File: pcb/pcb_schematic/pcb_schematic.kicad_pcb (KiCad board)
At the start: 2 copper layers, 35 parts, among them J1 Conn_ST_STDC14, J2 USB_B_Micro, J3 Conn_02x02_Odd_Even, Q1 MMBT3904, Q2 MMBT3904, Q3 MMBT3904, U1 STM32G031K8Tx, U2 MIC5301-3.3YD5, U4 SSD1306 128 x 64 OLED (0x3C), Y1 Crystal

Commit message: the schmatic keeps chaning i wanna cry
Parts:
- removed C10, C7: 1uF CER, Capacitor_SMD:C_0805_2012Metric
- removed C5: 4.7nF 1KV, Capacitor_SMD:C_0805_2012Metric
- removed C9: 0.01uF, Capacitor_SMD:C_0805_2012Metric
- removed J2: USB_B_Micro, Connector_USB:USB_Micro-B_Amphenol_10118194_Horizontal
- removed R1: 1M, Resistor_SMD:R_0805_2012Metric
- removed R11: 10K, Resistor_SMD:R_0805_2012Metric
- removed R3: 1.1k, Resistor_SMD:R_0805_2012Metric
- removed R4: 330, Resistor_SMD:R_0805_2012Metric
- added C14: 10uF, Capacitor_SMD:C_0805_2012Metric, F.Cu at (184.7, 119.6)
- added C6: 4.7nF 1KV, Capacitor_SMD:C_0805_2012Metric, F.Cu at (180.2, 116.6)
- added C8: 10uF, Capacitor_SMD:C_0805_2012Metric, F.Cu at (180.2, 119.6)
- added D1: CLMVC-FKA-CLBDGL7LBB79353, RGB_LED:LED_CLMVC-FKA-CLBDGL7LBB79353, F.Cu at (148.3, 41.6)
- added J4: USB_B_Micro, Connector_USB:USB_Micro-B_Amphenol_10118194_Horizontal, F.Cu at (178.2, 75.0)
- added R12: 10K, Resistor_SMD:R_0805_2012Metric, F.Cu at (178.0, 105.8)
- added U5: TCS34725 (0x29), Sensor:TCS34725, F.Cu at (149.8, 73.4)
- R2: value 1k -> 1M
- R5: value 1k -> 470
- R6: value 1.1k -> 220
- R7: value 330 -> 51
- U2: value MIC5301-3.3YD5 -> NCP1117-3.3_SOT223; footprint Package_TO_SOT_SMD:TSOT-23-5 -> Package_TO_SOT_SMD:SOT-223-3_TabPin2
- moved H1 165.5 mm to (274.7, 20.4)
- moved H2 165.5 mm to (274.7, 28.3)
- moved H3 165.5 mm to (274.7, 36.2)
- moved H4 165.5 mm to (274.7, 44.2)
- moved R10 74.4 mm to (178.0, 102.8)
- moved R8 74.4 mm to (178.0, 96.9)
- moved R9 74.4 mm to (178.0, 99.9)
- moved U2 67.9 mm to (185.1, 106.4)
- moved Y1 53.7 mm to (112.0, 75.7), turned to 90 degrees
- moved R5 52.1 mm to (149.0, 48.3)
- moved R6 52.1 mm to (149.0, 51.3)
- moved R7 52.1 mm to (149.0, 54.2)
- moved C11 51.2 mm to (184.7, 113.6)
- moved C12 51.2 mm to (184.7, 116.6)
- moved Q1 45.5 mm to (143.6, 46.7)
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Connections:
- Q2 pad 1: unconnected-(Q2-B-Pad1) -> Net-(Q2-B)
- Q3 pad 1: unconnected-(Q3-B-Pad1) -> Net-(Q3-B)
- R10 pad 2: unconnected-(R10-Pad2) -> Net-(Q3-B)
- R2 pad 1: unconnected-(R2-Pad1) -> Net-(J4-Shield)
- R2 pad 2: unconnected-(R2-Pad2) -> GND
- R9 pad 2: unconnected-(R9-Pad2) -> Net-(Q2-B)
- U1 pad 13: PWM1 -> unconnected-(U1-PA6-Pad13)
- U1 pad 14: PWM2 -> unconnected-(U1-PA7-Pad14)
- U1 pad 18: PWM3 -> PWM1
- U1 pad 22: unconnected-(U1-PA9/PA11-Pad22) -> PWM2
- U1 pad 23: unconnected-(U1-PA10/PA12-Pad23) -> PWM3
- U2 pad 1: VBUS -> GND
- U2 pad 2: GND -> +3.3V
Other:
- board outline added: 20.3 x 20.3 mm

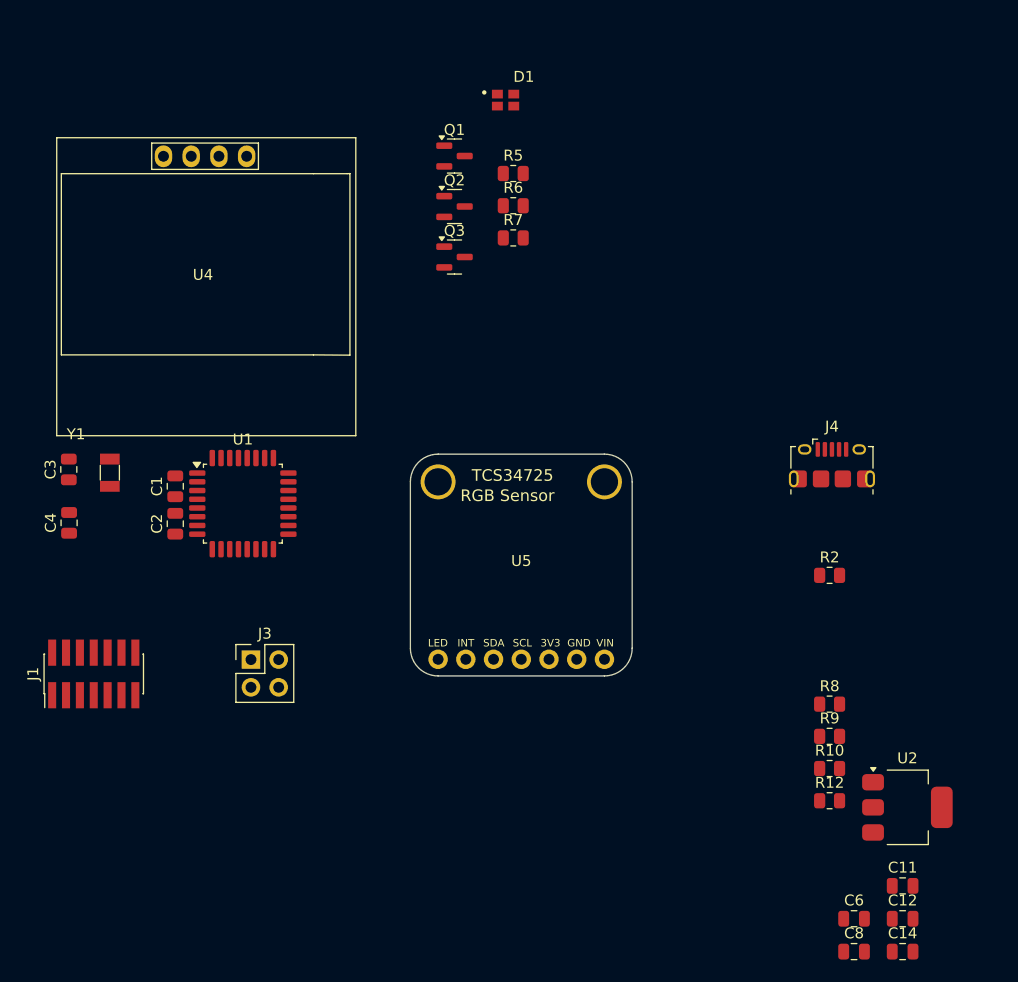
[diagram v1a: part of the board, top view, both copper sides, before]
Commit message: Components are laid out
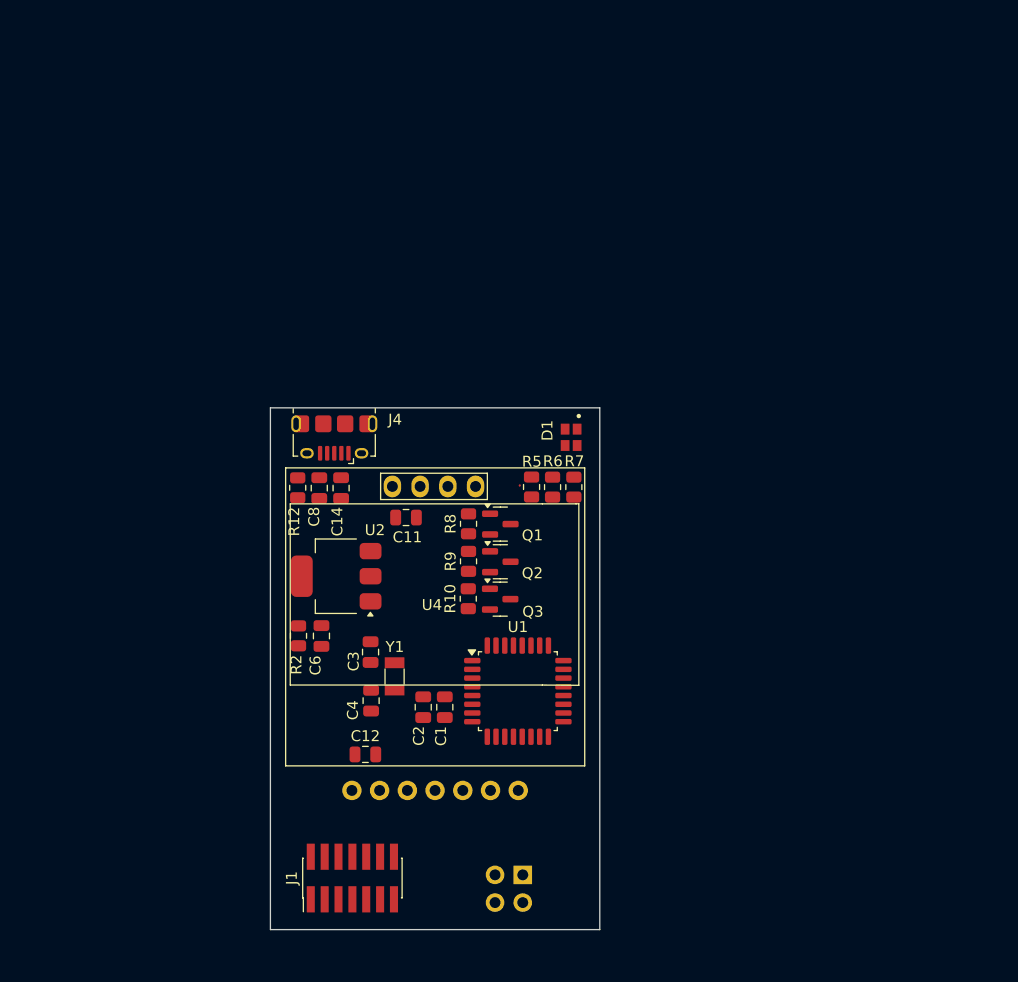
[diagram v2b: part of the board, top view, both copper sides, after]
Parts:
- J3, U5: moved to B.Cu
- moved C14 66.7 mm to (133.2, 77.1), turned to -90 degrees
- moved C8 64.8 mm to (131.2, 77.1), turned to 90 degrees
- moved C11 56.6 mm to (139.2, 79.8), turned to 180 degrees
- moved R12 56.5 mm to (129.2, 77.1), turned to 90 degrees
- moved U2 56.5 mm to (132.8, 85.2), turned to 180 degrees
- moved C6 55.2 mm to (131.4, 90.7), turned to 90 degrees
- moved C12 51.5 mm to (135.4, 101.5)
- moved R2 49.0 mm to (129.3, 90.7), turned to 90 degrees
- moved J4 45.7 mm to (132.6, 72.5), turned to 180 degrees
- moved R8 37.0 mm to (144.9, 80.4), turned to 90 degrees
- moved U4 36.8 mm to (141.5, 87.6)
- moved R9 36.8 mm to (144.9, 83.8), turned to 90 degrees
- moved R10 36.6 mm to (144.9, 87.3), turned to 90 degrees
- moved Q1 34.0 mm to (147.8, 80.4)
- moved Q2 32.8 mm to (147.8, 83.9)
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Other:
- board size 20.3 x 20.3 mm -> 30.2 x 47.8 mm
- copper layers 2 -> 4

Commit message: Update pcb_schematic.kicad_pcb
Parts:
- moved R8 39.3 mm to (183.7, 86.6)
- moved Q1 36.8 mm to (184.6, 83.0), turned to 90 degrees
- moved R9 35.5 mm to (180.2, 86.6)
- moved R12 34.3 mm to (163.5, 79.3)
- moved C8 34.3 mm to (165.5, 79.3)
- moved R5 33.9 mm to (184.5, 79.2)
- moved R2 33.8 mm to (161.1, 79.2), turned to -90 degrees
- moved Q2 33.3 mm to (181.1, 83.0), turned to 90 degrees
- moved U2 32.0 mm to (164.7, 87.0)
- moved R10 31.8 mm to (176.6, 86.6)
- moved J1 31.4 mm to (165.6, 114.1)
- moved J3 31.4 mm to (181.2, 113.8)
- moved Y1 30.2 mm to (168.3, 94.6)
- moved Q3 30.1 mm to (177.6, 83.0), turned to 90 degrees
- moved C4 30.1 mm to (166.1, 96.8)
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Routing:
- net Net-(J4-Shield): track 0.00 -> 17.2 mm
- net PWM1: track 0.00 -> 15.0 mm
- net PWM3: track 0.00 -> 13.9 mm
- net PWM2: track 0.00 -> 13.0 mm
- net GND: track 0.00 -> 12.9 mm, vias 0 -> 1
- net +3.3V: track 0.00 -> 11.1 mm
- net Net-(U1-PC14): track 0.00 -> 9.97 mm
- net Net-(U1-PC15): track 0.00 -> 9.82 mm
- net Net-(D1-Pad4): track 0.00 -> 8.75 mm
- net INT: track 0.00 -> 6.23 mm
- net LED: track 0.00 -> 5.84 mm
- net Net-(D1-Pad3): track 0.03 -> 4.79 mm
- net VBUS: track 0.00 -> 4.28 mm
- net Net-(D1-Pad2): track 0.00 -> 2.89 mm
- net Net-(Q1-C): track 0.00 -> 1.94 mm
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- added copper zone on In1.Cu, net GND

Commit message: Update pcb_schematic.kicad_pcb
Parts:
- moved C14 9.83 mm to (168.2, 86.3), turned to 90 degrees
- moved U2 2.78 mm to (162.6, 85.2)
- moved C1 0.83 mm to (172.5, 98.6)
- moved C2 0.83 mm to (170.5, 98.6)
- moved C3 0.83 mm to (166.0, 93.1)
- moved Y1 0.83 mm to (168.3, 95.4)
- moved C4 0.83 mm to (166.1, 97.6)
- moved U1 0.83 mm to (179.3, 98.0)
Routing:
- net SCL: track 0.00 -> 49.9 mm, vias 0 -> 2
- net SDA: track 0.00 -> 49.9 mm, vias 0 -> 1
- net GND: track 12.9 -> 35.0 mm, vias 1 -> 15
- net Net-(J1-~{RST}): track 0.00 -> 12.2 mm, vias 0 -> 1
- net +3.3V: track 11.1 -> 19.4 mm, vias 0 -> 4
- net Net-(J3-Pin_3): track 0.00 -> 7.48 mm, vias 0 -> 2
- net VBUS: track 4.28 -> 9.58 mm
- added copper zone on In2.Cu, net +3.3V

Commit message: Update pcb_schematic.kicad_pcb
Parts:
- moved J3 5.75 mm to (175.6, 112.8), turned to -90 degrees
- moved J1 2.40 mm to (168.0, 114.1)
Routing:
- net Net-(J1-JCLK/SWCLK): track 0.00 -> 34.9 mm, vias 0 -> 2
- net Net-(J1-JTMS/SWDIO): track 0.14 -> 31.6 mm, vias 0 -> 2
- net Net-(J3-Pin_1): track 0.00 -> 11.1 mm, vias 0 -> 1
- net Net-(J1-VCP_RX): track 0.00 -> 10.3 mm, vias 0 -> 1
- net +3.3V: track 19.4 -> 28.6 mm, vias 4 -> 6
- net Net-(J1-~{RST}): track 12.2 -> 18.2 mm, vias 1 -> 0
- net Net-(J1-VCP_TX): track 0.00 -> 5.54 mm, vias 0 -> 2
- net GND: track 35.0 -> 40.4 mm, vias 15 -> 18
- net Net-(J3-Pin_3): track 7.48 -> 11.1 mm, vias 2 -> 1
- net INT: track 6.23 -> 7.30 mm
- net LED: track 5.84 -> 5.01 mm
- net PWM3: track 14.2 -> 14.8 mm
- net Net-(J4-Shield): track 17.0 -> 17.6 mm

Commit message: before i change many thing
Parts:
- moved H3 144.0 mm to (154.5, 115.5)
- moved H1 131.9 mm to (154.5, 74.7)
- moved H4 111.6 mm to (188.8, 115.5)
- moved H2 97.5 mm to (188.9, 74.7)
- moved C6 2.64 mm to (156.7, 80.4)
- moved R2 0.83 mm to (160.2, 79.2)
- moved U2 0.65 mm to (162.8, 85.8)
- moved J4 0.35 mm to (162.4, 74.2)
- moved C14 0.24 mm to (168.4, 86.3)
- moved D1 0.18 mm to (184.2, 74.6)
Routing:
- net Net-(J4-Shield): track 17.6 -> 12.3 mm
- net GND: track 40.4 -> 39.4 mm
- net +3.3V: track 28.6 -> 28.1 mm
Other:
- board size 30.2 x 47.8 mm -> 41.4 x 47.8 mm
- board text added: "Jaedyn Carbonell CMPE2750 RGB Reader"

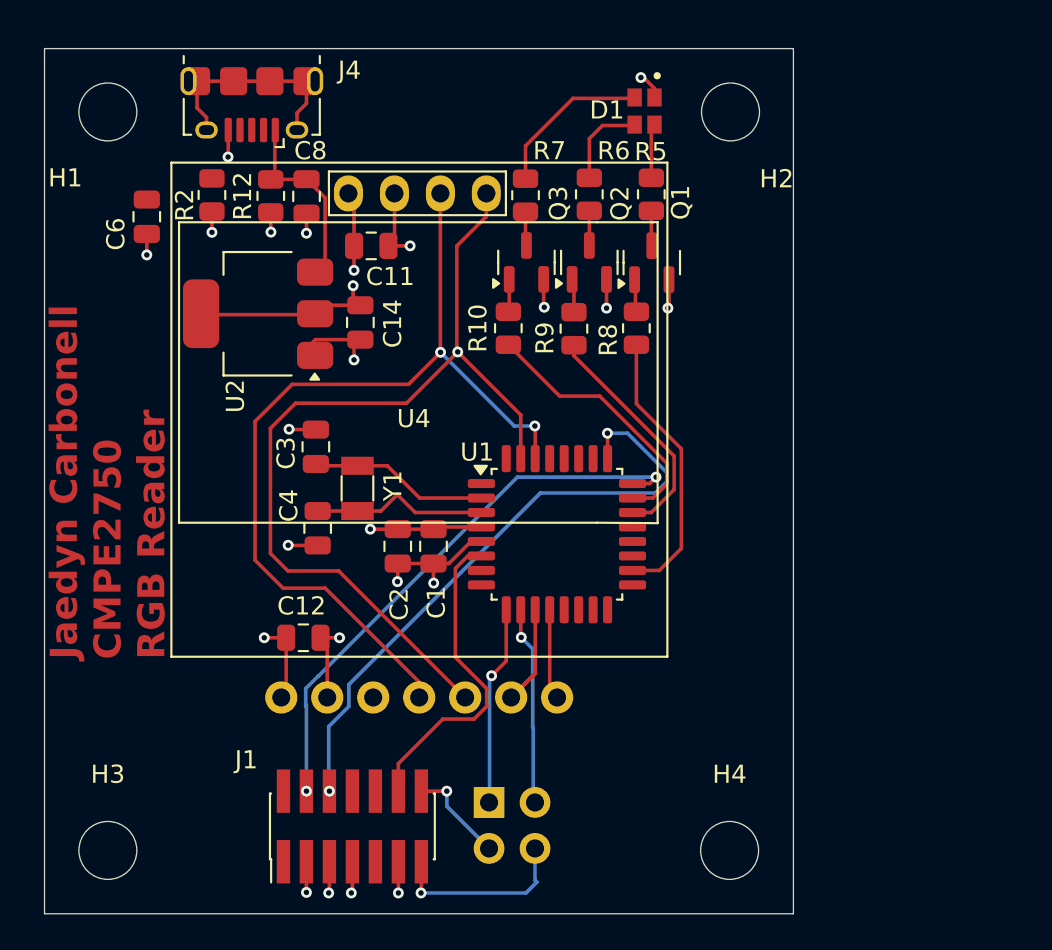
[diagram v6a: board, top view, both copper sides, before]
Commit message: moved rbg led
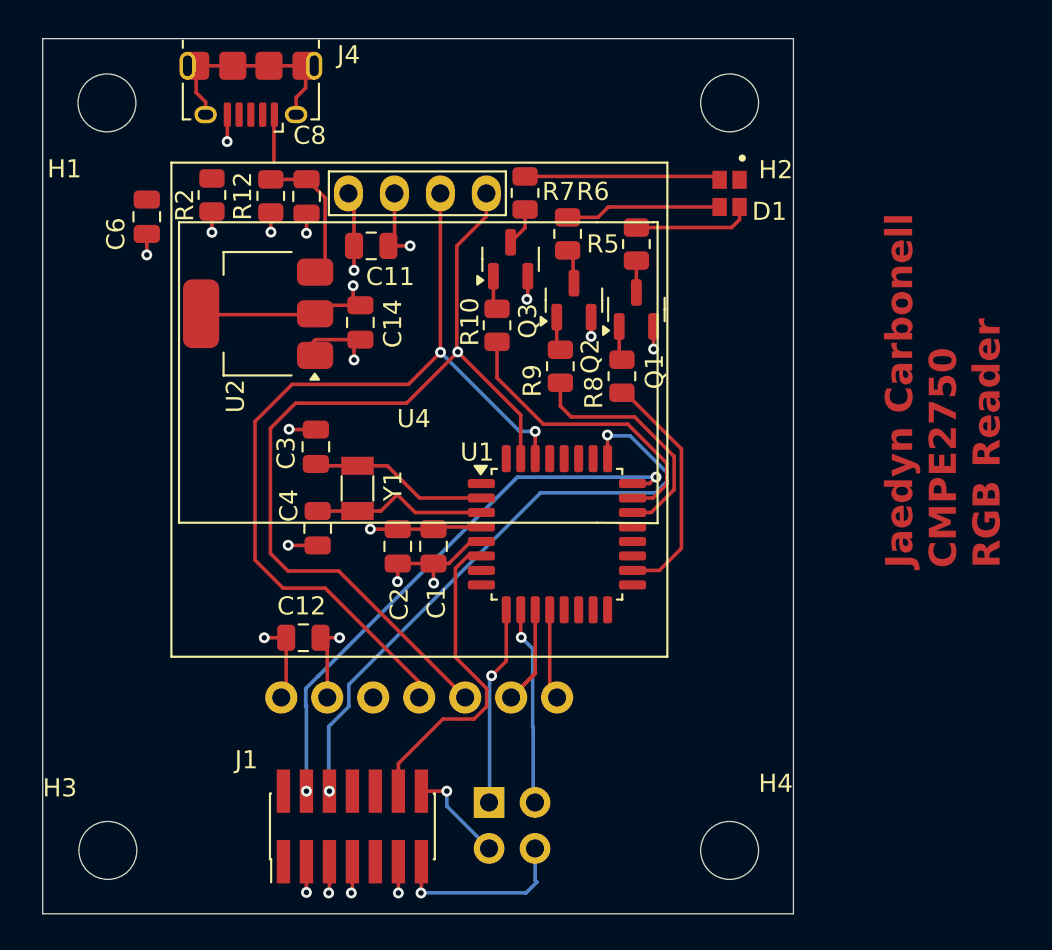
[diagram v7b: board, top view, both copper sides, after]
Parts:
- moved D1 6.54 mm to (188.8, 79.2)
- moved R5 2.87 mm to (183.7, 82.0)
- moved R8 2.77 mm to (182.9, 89.2)
- moved Q1 2.72 mm to (183.7, 85.6)
- moved R6 2.50 mm to (179.9, 81.4)
- moved Q2 2.25 mm to (180.2, 85.0)
- moved R9 2.21 mm to (179.5, 88.7)
- moved Q3 0.89 mm to (176.8, 82.8)
- moved J4 0.85 mm to (162.4, 73.4)
- moved R10 0.65 mm to (176.0, 86.4)
- moved H1 0.50 mm to (154.4, 74.2)
- moved H2 0.50 mm to (188.8, 74.2)
- moved R7 0.13 mm to (177.6, 79.1)
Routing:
- net Net-(D1-Pad3): track 4.79 -> 8.64 mm
- net Net-(D1-Pad2): track 2.89 -> 6.58 mm
- net PWM1: track 15.5 -> 13.3 mm
- net Net-(D1-Pad4): track 8.75 -> 10.8 mm
- net PWM3: track 14.8 -> 16.7 mm
- net +3.3V: track 28.1 -> 26.5 mm, vias 6 -> 5
- net GND: track 39.4 -> 38.2 mm
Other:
- board size 41.4 x 47.8 mm -> 41.5 x 48.4 mm

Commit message: Created pcb desgin, need to rid of all warning
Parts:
- moved J4 12.3 mm to (153.7, 82.1), turned to -90 degrees
- moved R2 11.3 mm to (153.6, 88.4)
- moved C6 7.92 mm to (156.9, 88.3)
- moved C14 7.89 mm to (163.8, 79.9), turned to 180 degrees
- moved R12 6.28 mm to (157.2, 79.9), turned to -90 degrees
- moved C8 5.51 mm to (160.0, 79.9), turned to 180 degrees
- moved U2 0.97 mm to (161.9, 85.5), turned to -90 degrees
- moved C11 0.10 mm to (169.2, 82.0)
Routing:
- net Net-(J4-Shield): track 12.3 -> 18.0 mm
- net +3.3V: track 26.5 -> 30.9 mm, vias 5 -> 6
- net VBUS: track 10.0 -> 7.86 mm
- net GND: track 38.2 -> 39.1 mm
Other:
- board text added: "RGB Reader-CMPE2750 Jaedyn Carbonell"
- board text removed: "Jaedyn Carbonell CMPE2750 RGB Reader"
